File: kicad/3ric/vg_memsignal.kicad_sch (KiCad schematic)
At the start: 6 parts

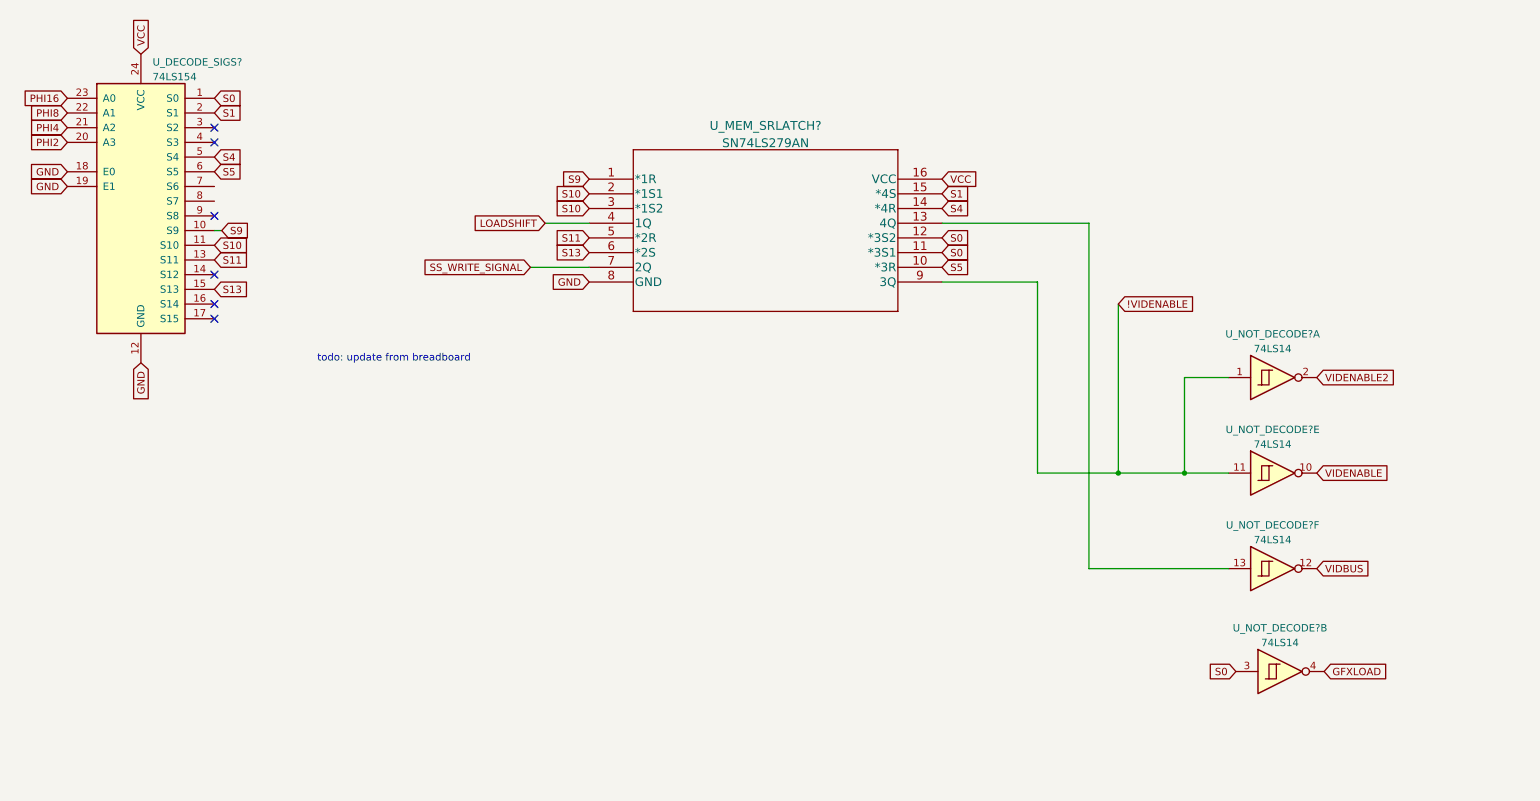
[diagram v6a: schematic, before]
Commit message: update schematic based on breadboard
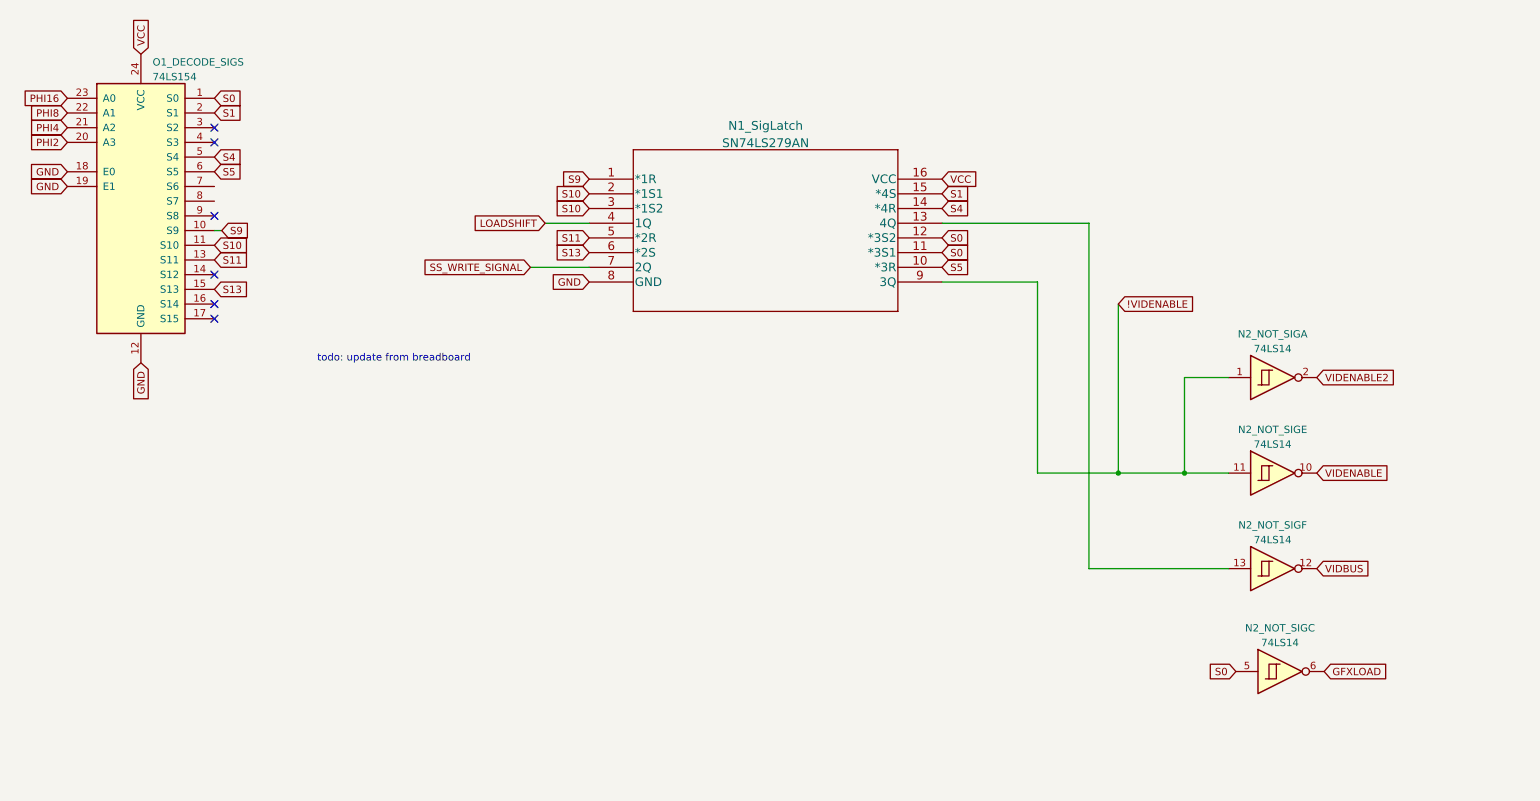
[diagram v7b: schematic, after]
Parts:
- gave numbers to parts that had none: 3
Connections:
- net GFXLOAD: now also N2_NOT_SIG.6; no longer N2_NOT_SIG.4
- net S0: now also N2_NOT_SIG.5; no longer N2_NOT_SIG.3
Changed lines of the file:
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@@
 		(dnp no)
 		(fields_autoplaced yes)
-		(property "Reference" "U_NOT_DECODE?"
+		(property "Reference" "N2_NOT_SIG"
 			(at 232.41 101.7102 0)
 			(effects
@@
 			(project "3ric"
 				(path "/e63e39d7-6ac0-4ffd-8aa3-1841a4541b55/b61474be-3832-4b6c-a3a4-928ac814faf5"
-					(reference "U_NOT_DECODE?")
+					(reference "N2_NOT_SIG")
 					(unit 5)
 				)
@@
 		(dnp no)
 		(fields_autoplaced yes)
-		(property "Reference" "U_DECODE_SIGS?"
+		(property "Reference" "O1_DECODE_SIGS"
 			(at 38.8494 38.2102 0)
 			(effects
@@
 			(project "3ric"
 				(path "/e63e39d7-6ac0-4ffd-8aa3-1841a4541b55/b61474be-3832-4b6c-a3a4-928ac814faf5"
-					(reference "U_DECODE_SIGS?")
+					(reference "O1_DECODE_SIGS")
 					(unit 1)
 				)
@@
 		(dnp no)
 		(fields_autoplaced yes)
-		(property "Reference" "U_NOT_DECODE?"
+		(property "Reference" "N2_NOT_SIG"
 			(at 232.41 85.2002 0)
 			(effects
@@
 			(project "3ric"
 				(path "/e63e39d7-6ac0-4ffd-8aa3-1841a4541b55/b61474be-3832-4b6c-a3a4-928ac814faf5"
-					(reference "U_NOT_DECODE?")
+					(reference "N2_NOT_SIG")
 					(unit 1)
 				)
@@
 		(lib_id "74xx:74LS14")
 		(at 233.68 143.51 0)
-		(unit 2)
+		(unit 3)
 		(exclude_from_sim no)
 		(in_bom yes)
@@
 		(dnp no)
 		(fields_autoplaced yes)
-		(property "Reference" "U_NOT_DECODE?"
+		(property "Reference" "N2_NOT_SIG"
 			(at 233.68 136.0002 0)
 			(effects
@@
 			(project "3ric"
 				(path "/e63e39d7-6ac0-4ffd-8aa3-1841a4541b55/b61474be-3832-4b6c-a3a4-928ac814faf5"
-					(reference "U_NOT_DECODE?")
-					(unit 2)
+					(reference "N2_NOT_SIG")
+					(unit 3)
 				)
 			)
@@
 		(dnp no)
 		(fields_autoplaced yes)
-		(property "Reference" "U_NOT_DECODE?"
+		(property "Reference" "N2_NOT_SIG"
 			(at 232.41 118.2202 0)
 			(effects
@@
 			(project "3ric"
 				(path "/e63e39d7-6ac0-4ffd-8aa3-1841a4541b55/b61474be-3832-4b6c-a3a4-928ac814faf5"
-					(reference "U_NOT_DECODE?")
+					(reference "N2_NOT_SIG")
 					(unit 6)
 				)
@@
 		(dnp no)
 		(fields_autoplaced yes)
-		(property "Reference" "U_MEM_SRLATCH?"
+		(property "Reference" "N1_SigLatch"
 			(at 144.78 49.1924 0)
 			(effects
@@
 			(project "3ric"
 				(path "/e63e39d7-6ac0-4ffd-8aa3-1841a4541b55/b61474be-3832-4b6c-a3a4-928ac814faf5"
-					(reference "U_MEM_SRLATCH?")
+					(reference "N1_SigLatch")
 					(unit 1)
 				)

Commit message: cleaning up of the schematic
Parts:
- added unit 2 of N2_NOT_SIG1
- added unit 4 of N2_NOT_SIG1
- renumbered N1_SigLatch to N1_SigLatch1, N2_NOT_SIG to N2_NOT_SIG1, O1_DECODE_SIGS to O1_DECODE_SIGS1
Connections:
- no-connect marks 6 -> 12
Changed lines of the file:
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@@
+	)
+	(no_connect
+		(at 240.03 160.02)
 	)
 	(no_connect
@@
 	(no_connect
 		(at 49.53 64.77)
+	)
+	(no_connect
+		(at 260.35 160.02)
+	)
+	(no_connect
+		(at 49.53 59.69)
+	)
+	(no_connect
+		(at 224.79 160.02)
+	)
+	(no_connect
+		(at 49.53 62.23)
+	)
+	(no_connect
+		(at 275.59 160.02)
 	)
 	(wire
@@
 		(dnp no)
 		(fields_autoplaced yes)
-		(property "Reference" "N2_NOT_SIG"
+		(property "Reference" "N2_NOT_SIG1"
 			(at 232.41 101.7102 0)
 			(effects
@@
 			(project "3ric"
 				(path "/e63e39d7-6ac0-4ffd-8aa3-1841a4541b55/b61474be-3832-4b6c-a3a4-928ac814faf5"
-					(reference "N2_NOT_SIG")
+					(reference "N2_NOT_SIG1")
 					(unit 5)
 				)
@@
 		(dnp no)
 		(fields_autoplaced yes)
-		(property "Reference" "O1_DECODE_SIGS"
+		(property "Reference" "O1_DECODE_SIGS1"
 			(at 38.8494 38.2102 0)
 			(effects
@@
 			(project "3ric"
 				(path "/e63e39d7-6ac0-4ffd-8aa3-1841a4541b55/b61474be-3832-4b6c-a3a4-928ac814faf5"
-					(reference "O1_DECODE_SIGS")
+					(reference "O1_DECODE_SIGS1")
 					(unit 1)
 				)
@@
 		(dnp no)
 		(fields_autoplaced yes)
-		(property "Reference" "N2_NOT_SIG"
+		(property "Reference" "N2_NOT_SIG1"
 			(at 232.41 85.2002 0)
 			(effects
@@
 			(project "3ric"
 				(path "/e63e39d7-6ac0-4ffd-8aa3-1841a4541b55/b61474be-3832-4b6c-a3a4-928ac814faf5"
-					(reference "N2_NOT_SIG")
+					(reference "N2_NOT_SIG1")
 					(unit 1)
 				)
@@
 		(dnp no)
 		(fields_autoplaced yes)
-		(property "Reference" "N2_NOT_SIG"
+		(property "Reference" "N2_NOT_SIG1"
 			(at 233.68 136.0002 0)
 			(effects
@@
 			(project "3ric"
 				(path "/e63e39d7-6ac0-4ffd-8aa3-1841a4541b55/b61474be-3832-4b6c-a3a4-928ac814faf5"
-					(reference "N2_NOT_SIG")
+					(reference "N2_NOT_SIG1")
 					(unit 3)
+				)
+			)
+		)
+	)
+	(symbol
+		(lib_id "74xx:74LS14")
+		(at 232.41 160.02 0)
+		(unit 2)
+		(exclude_from_sim no)
+		(in_bom yes)
+		(on_board yes)
+		(dnp no)
+		(fields_autoplaced yes)
+		(property "Reference" "N2_NOT_SIG1"
+			(at 232.41 152.5102 0)
+			(effects
+				(font
+					(size 1.27 1.27)
+				)
+			)
+		)
+		(property "Value" "74LS14"
+			(at 232.41 155.0471 0)
+			(effects
+				(font
+					(size 1.27 1.27)
+				)
+			)
+		)
+		(property "Footprint" "Package_DIP:DIP-14_W7.62mm_Socket"
+			(at 232.41 160.02 0)
+			(effects
+				(font
+					(size 1.27 1.27)
+				)
+				(hide yes)
+			)
+		)
+		(property "Datasheet" "http://www.ti.com/lit/gpn/sn74LS14"
+			(at 232.41 160.02 0)
+			(effects
+				(font
+					(size 1.27 1.27)
+				)
+				(hide yes)
+			)
+		)
+		(property "Description" ""
+			(at 232.41 160.02 0)
+			(effects
+				(font
+					(size 1.27 1.27)
+				)
+				(hide yes)
+			)
+		)
+		(pin "1"
+		)
+		(pin "2"
+		)
+		(pin "3"
+		)
+		(pin "4"
+		)
+		(pin "5"
+		)
+		(pin "6"
+		)
+		(pin "8"
+		)
+		(pin "9"
+		)
+		(pin "10"
+		)
+		(pin "11"
+		)
+		(pin "12"
+		)
+		(pin "13"
+		)
+		(pin "14"
+		)
+		(pin "7"
+		)
+		(instances
+			(project "3ric"
+				(path "/e63e39d7-6ac0-4ffd-8aa3-1841a4541b55/b61474be-3832-4b6c-a3a4-928ac814faf5"
+					(reference "N2_NOT_SIG1")
+					(unit 2)
 				)
 			)
@@
 		(dnp no)
 		(fields_autoplaced yes)
-		(property "Reference" "N2_NOT_SIG"
+		(property "Reference" "N2_NOT_SIG1"
 			(at 232.41 118.2202 0)
 			(effects
@@
 			(project "3ric"
 				(path "/e63e39d7-6ac0-4ffd-8aa3-1841a4541b55/b61474be-3832-4b6c-a3a4-928ac814faf5"
-					(reference "N2_NOT_SIG")
+					(reference "N2_NOT_SIG1")
 					(unit 6)
+				)
+			)
+		)
+	)
+	(symbol
+		(lib_id "74xx:74LS14")
+		(at 267.97 160.02 0)
+		(unit 4)
+		(exclude_from_sim no)
+		(in_bom yes)
+		(on_board yes)
+		(dnp no)
+		(fields_autoplaced yes)
+		(property "Reference" "N2_NOT_SIG1"
+			(at 267.97 152.5102 0)
+			(effects
+				(font
+					(size 1.27 1.27)
+				)
+			)
+		)
+		(property "Value" "74LS14"
+			(at 267.97 155.0471 0)
+			(effects
+				(font
+					(size 1.27 1.27)
+				)
+			)
+		)
+		(property "Footprint" "Package_DIP:DIP-14_W7.62mm_Socket"
+			(at 267.97 160.02 0)
+			(effects
+				(font
+					(size 1.27 1.27)
+				)
+				(hide yes)
+			)
+		)
+		(property "Datasheet" "http://www.ti.com/lit/gpn/sn74LS14"
+			(at 267.97 160.02 0)
+			(effects
+				(font
+					(size 1.27 1.27)
+				)
+				(hide yes)
+			)
+		)
+		(property "Description" ""
+			(at 267.97 160.02 0)
+			(effects
+				(font
+					(size 1.27 1.27)
+				)
+				(hide yes)
+			)
+		)
+		(pin "1"
+		)
+		(pin "2"
+		)
+		(pin "3"
+		)
+		(pin "4"
+		)
+		(pin "5"
+		)
+		(pin "6"
+		)
+		(pin "8"
+		)
+		(pin "9"
+		)
+		(pin "10"
+		)
+		(pin "11"
+		)
+		(pin "12"
+		)
+		(pin "13"
+		)
+		(pin "14"
+		)
+		(pin "7"
+		)
+		(instances
+			(project "3ric"
+				(path "/e63e39d7-6ac0-4ffd-8aa3-1841a4541b55/b61474be-3832-4b6c-a3a4-928ac814faf5"
+					(reference "N2_NOT_SIG1")
+					(unit 4)
 				)
 			)
@@
 		(dnp no)
 		(fields_autoplaced yes)
-		(property "Reference" "N1_SigLatch"
+		(property "Reference" "N1_SigLatch1"
 			(at 144.78 49.1924 0)
 			(effects
@@
 			(project "3ric"
 				(path "/e63e39d7-6ac0-4ffd-8aa3-1841a4541b55/b61474be-3832-4b6c-a3a4-928ac814faf5"
-					(reference "N1_SigLatch")
+					(reference "N1_SigLatch1")
 					(unit 1)
 				)
